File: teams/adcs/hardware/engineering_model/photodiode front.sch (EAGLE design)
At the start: 15 parts, among them U1 LTC2483IDD

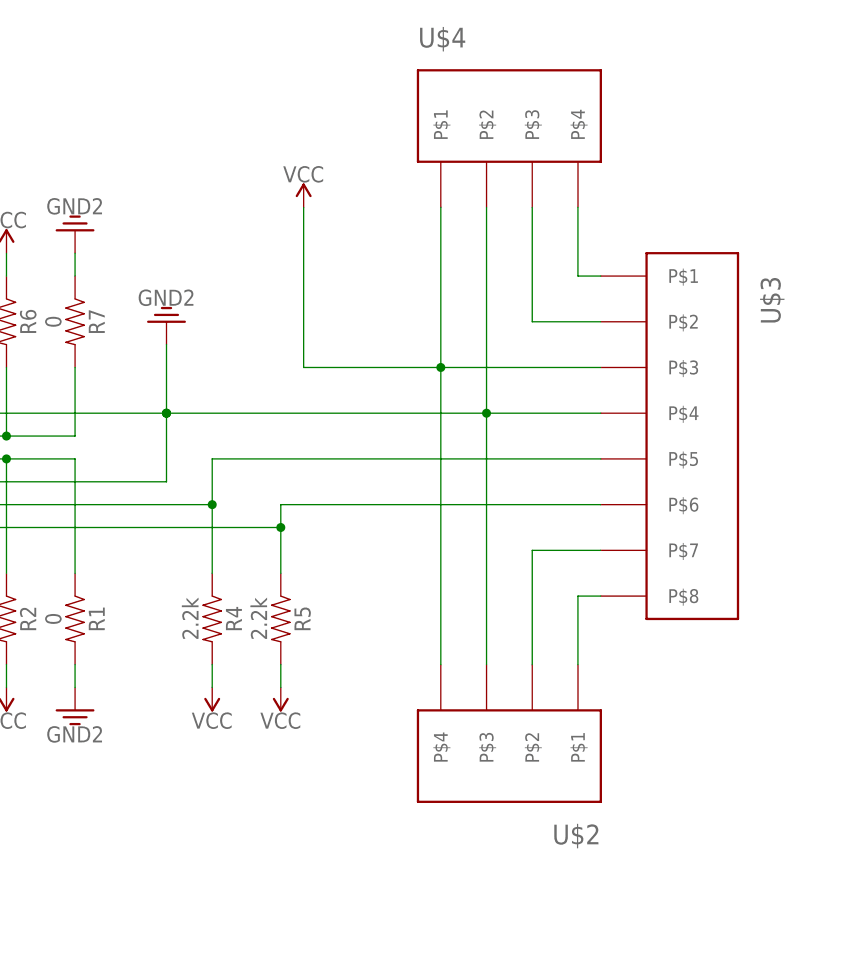
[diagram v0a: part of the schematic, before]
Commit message: Fixed front photodiode board
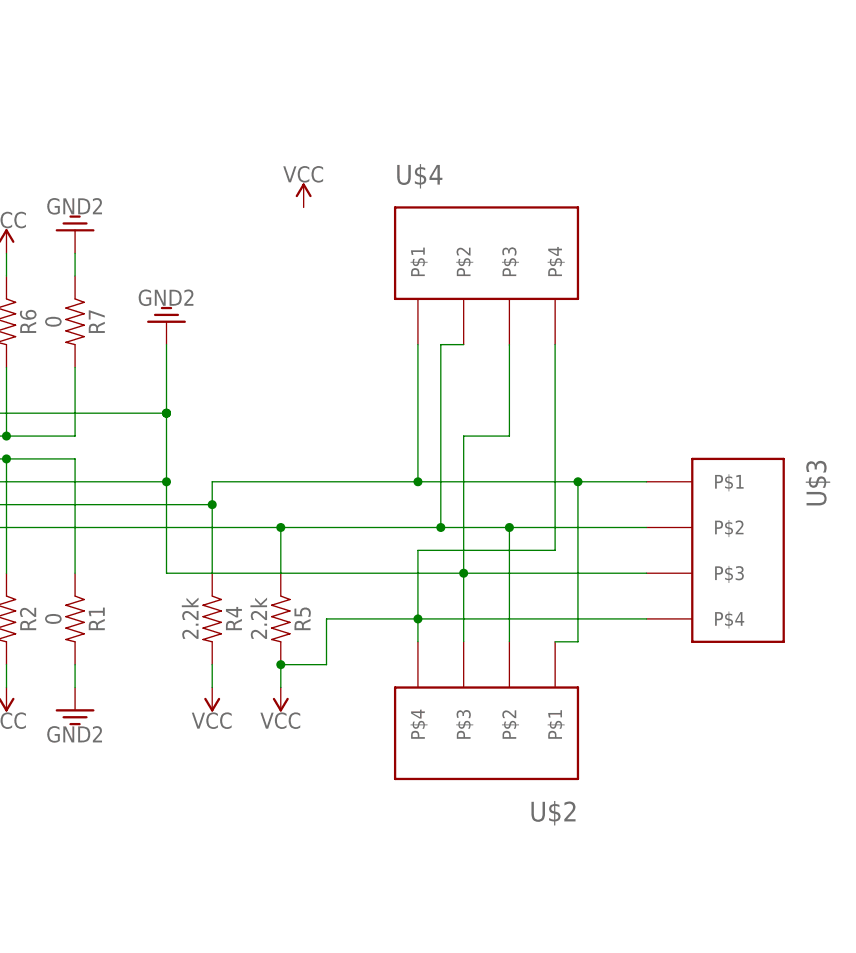
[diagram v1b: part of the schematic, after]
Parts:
- U$3: value PICOLOCK_8 -> PICOLOCK_4PICOLOCK_4; device DubSat1 Components:PICOLOCK_8 -> DubSat1 Components:PICOLOCK_4PICOLOCK_4
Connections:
- removed net N$1: U$3.P$2, U$4.P$3
- removed net N$2: U$3.P$1, U$4.P$4
- removed net N$3: U$2.P$1, U$3.P$8
- removed net N$4: U$2.P$2, U$3.P$7
- net GND: now also U$3.P$3, U$4.P$3; no longer U$3.P$4, U$4.P$2
- net SCL: now also U$2.P$2, U$3.P$2, U$4.P$2; no longer U$3.P$6
- net SDA: now also U$2.P$1, U$3.P$1, U$4.P$1; no longer U$3.P$5
- net VCC: now also U$3.P$4, U$4.P$4; no longer U$3.P$3, U$4.P$1
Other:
- moved on the sheet: U$2, U$4
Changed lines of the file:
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@@
 <part name="GND" library="SparkFun-PowerSymbols" deviceset="GND2" device=""/>
 <part name="C2" library="SparkFun-Capacitors" deviceset="0.1UF" device="-0603-100V-10%" value="1uF"/>
-<part name="U$3" library="DubSat1 Components" deviceset="PICOLOCK_8" device=""/>
 <part name="U$2" library="DubSat1 Components" deviceset="PICOLOCK_4" device="PICOLOCK_4"/>
 <part name="U$4" library="DubSat1 Components" deviceset="PICOLOCK_4" device="PICOLOCK_4"/>
 <part name="SUPPLY9" library="SparkFun-PowerSymbols" deviceset="VCC" device=""/>
+<part name="U$3" library="DubSat1 Components" deviceset="PICOLOCK_4" device="PICOLOCK_4"/>
 </parts>
 <sheets>
@@
 <instance part="GND" gate="G$1" x="129.54" y="78.74" rot="R180"/>
 <instance part="C2" gate="G$1" x="33.02" y="76.2"/>
-<instance part="U$3" gate="G$1" x="182.88" y="71.12" rot="R270"/>
-<instance part="U$2" gate="G$1" x="162.56" y="35.56" rot="R180"/>
-<instance part="U$4" gate="G$1" x="172.72" y="96.52"/>
+<instance part="U$2" gate="G$1" x="160.02" y="38.1" rot="R180"/>
+<instance part="U$4" gate="G$1" x="170.18" y="81.28"/>
 <instance part="SUPPLY9" gate="G$1" x="144.78" y="91.44"/>
+<instance part="U$3" gate="G$1" x="187.96" y="48.26" rot="R270"/>
 </instances>
 <busses>
@@
 <pinref part="SUPPLY5" gate="G$1" pin="VCC"/>
 <wire x1="142.24" y1="40.64" x2="142.24" y2="38.1" width="0.1524" layer="91"/>
-</segment>
-<segment>
-<pinref part="SUPPLY9" gate="G$1" pin="VCC"/>
-<pinref part="U$3" gate="G$1" pin="P$3"/>
-<wire x1="144.78" y1="91.44" x2="144.78" y2="73.66" width="0.1524" layer="91"/>
-<wire x1="144.78" y1="73.66" x2="160.02" y2="73.66" width="0.1524" layer="91"/>
-<pinref part="U$4" gate="G$1" pin="P$1"/>
-<wire x1="160.02" y1="73.66" x2="177.8" y2="73.66" width="0.1524" layer="91"/>
-<wire x1="160.02" y1="91.44" x2="160.02" y2="73.66" width="0.1524" layer="91"/>
-<junction x="160.02" y="73.66"/>
+<pinref part="U$3" gate="G$1" pin="P$4"/>
+<wire x1="157.48" y1="45.72" x2="147.32" y2="45.72" width="0.1524" layer="91"/>
+<wire x1="147.32" y1="45.72" x2="147.32" y2="40.64" width="0.1524" layer="91"/>
+<wire x1="147.32" y1="40.64" x2="142.24" y2="40.64" width="0.1524" layer="91"/>
+<junction x="142.24" y="40.64"/>
+<pinref part="U$4" gate="G$1" pin="P$4"/>
+<wire x1="172.72" y1="76.2" x2="172.72" y2="53.34" width="0.1524" layer="91"/>
 <pinref part="U$2" gate="G$1" pin="P$4"/>
-<wire x1="160.02" y1="40.64" x2="160.02" y2="73.66" width="0.1524" layer="91"/>
+<wire x1="172.72" y1="53.34" x2="157.48" y2="53.34" width="0.1524" layer="91"/>
+<wire x1="157.48" y1="53.34" x2="157.48" y2="45.72" width="0.1524" layer="91"/>
+<wire x1="157.48" y1="45.72" x2="157.48" y2="43.18" width="0.1524" layer="91"/>
+<wire x1="182.88" y1="45.72" x2="157.48" y2="45.72" width="0.1524" layer="91"/>
+<junction x="157.48" y="45.72"/>
 </segment>
 </net>
@@
 <pinref part="R5" gate="G$1" pin="1"/>
 <wire x1="142.24" y1="50.8" x2="142.24" y2="55.88" width="0.1524" layer="91"/>
-<pinref part="U$3" gate="G$1" pin="P$6"/>
-<wire x1="177.8" y1="58.42" x2="142.24" y2="58.42" width="0.1524" layer="91"/>
-<wire x1="142.24" y1="58.42" x2="142.24" y2="55.88" width="0.1524" layer="91"/>
+<pinref part="U$3" gate="G$1" pin="P$2"/>
+<wire x1="182.88" y1="55.88" x2="167.64" y2="55.88" width="0.1524" layer="91"/>
 <junction x="142.24" y="55.88"/>
+<pinref part="U$2" gate="G$1" pin="P$2"/>
+<wire x1="167.64" y1="55.88" x2="160.02" y2="55.88" width="0.1524" layer="91"/>
+<wire x1="160.02" y1="55.88" x2="142.24" y2="55.88" width="0.1524" layer="91"/>
+<wire x1="167.64" y1="43.18" x2="167.64" y2="55.88" width="0.1524" layer="91"/>
+<junction x="167.64" y="55.88"/>
+<pinref part="U$4" gate="G$1" pin="P$2"/>
+<wire x1="162.56" y1="76.2" x2="160.02" y2="76.2" width="0.1524" layer="91"/>
+<wire x1="160.02" y1="76.2" x2="160.02" y2="55.88" width="0.1524" layer="91"/>
+<junction x="160.02" y="55.88"/>
 </segment>
 </net>
@@
 <pinref part="R4" gate="G$1" pin="1"/>
 <wire x1="134.62" y1="50.8" x2="134.62" y2="58.42" width="0.1524" layer="91"/>
-<pinref part="U$3" gate="G$1" pin="P$5"/>
-<wire x1="177.8" y1="63.5" x2="134.62" y2="63.5" width="0.1524" layer="91"/>
-<wire x1="134.62" y1="63.5" x2="134.62" y2="58.42" width="0.1524" layer="91"/>
+<pinref part="U$3" gate="G$1" pin="P$1"/>
+<wire x1="182.88" y1="60.96" x2="175.26" y2="60.96" width="0.1524" layer="91"/>
+<wire x1="175.26" y1="60.96" x2="157.48" y2="60.96" width="0.1524" layer="91"/>
+<wire x1="157.48" y1="60.96" x2="134.62" y2="60.96" width="0.1524" layer="91"/>
+<wire x1="134.62" y1="60.96" x2="134.62" y2="58.42" width="0.1524" layer="91"/>
 <junction x="134.62" y="58.42"/>
+<pinref part="U$4" gate="G$1" pin="P$1"/>
+<wire x1="157.48" y1="76.2" x2="157.48" y2="60.96" width="0.1524" layer="91"/>
+<junction x="157.48" y="60.96"/>
+<pinref part="U$2" gate="G$1" pin="P$1"/>
+<wire x1="172.72" y1="43.18" x2="175.26" y2="43.18" width="0.1524" layer="91"/>
+<wire x1="175.26" y1="43.18" x2="175.26" y2="60.96" width="0.1524" layer="91"/>
+<junction x="175.26" y="60.96"/>
 </segment>
 </net>
@@
 <wire x1="109.22" y1="68.58" x2="129.54" y2="68.58" width="0.1524" layer="91"/>
 <junction x="129.54" y="68.58"/>
-<pinref part="U$3" gate="G$1" pin="P$4"/>
-<wire x1="177.8" y1="68.58" x2="165.1" y2="68.58" width="0.1524" layer="91"/>
+<pinref part="U$3" gate="G$1" pin="P$3"/>
+<wire x1="162.56" y1="50.8" x2="129.54" y2="50.8" width="0.1524" layer="91"/>
+<wire x1="129.54" y1="50.8" x2="129.54" y2="60.96" width="0.1524" layer="91"/>
+<junction x="129.54" y="60.96"/>
 <pinref part="U$2" gate="G$1" pin="P$3"/>
-<wire x1="165.1" y1="68.58" x2="129.54" y2="68.58" width="0.1524" layer="91"/>
-<wire x1="165.1" y1="40.64" x2="165.1" y2="68.58" width="0.1524" layer="91"/>
-<junction x="165.1" y="68.58"/>
-<pinref part="U$4" gate="G$1" pin="P$2"/>
-<wire x1="165.1" y1="91.44" x2="165.1" y2="68.58" width="0.1524" layer="91"/>
+<wire x1="162.56" y1="43.18" x2="162.56" y2="50.8" width="0.1524" layer="91"/>
+<pinref part="U$4" gate="G$1" pin="P$3"/>
+<wire x1="162.56" y1="50.8" x2="162.56" y2="66.04" width="0.1524" layer="91"/>
+<wire x1="162.56" y1="66.04" x2="167.64" y2="66.04" width="0.1524" layer="91"/>
+<wire x1="167.64" y1="66.04" x2="167.64" y2="76.2" width="0.1524" layer="91"/>
+<wire x1="182.88" y1="50.8" x2="162.56" y2="50.8" width="0.1524" layer="91"/>
+<junction x="162.56" y="50.8"/>
 </segment>
 <segment>
@@
 </segment>
 </net>
-<net name="N$1" class="0">
-<segment>
-<pinref part="U$3" gate="G$1" pin="P$2"/>
-<pinref part="U$4" gate="G$1" pin="P$3"/>
-<wire x1="177.8" y1="78.74" x2="170.18" y2="78.74" width="0.1524" layer="91"/>
-<wire x1="170.18" y1="78.74" x2="170.18" y2="91.44" width="0.1524" layer="91"/>
-</segment>
-</net>
-<net name="N$2" class="0">
-<segment>
-<pinref part="U$3" gate="G$1" pin="P$1"/>
-<pinref part="U$4" gate="G$1" pin="P$4"/>
-<wire x1="177.8" y1="83.82" x2="175.26" y2="83.82" width="0.1524" layer="91"/>
-<wire x1="175.26" y1="83.82" x2="175.26" y2="91.44" width="0.1524" layer="91"/>
-</segment>
-</net>
-<net name="N$3" class="0">
-<segment>
-<pinref part="U$3" gate="G$1" pin="P$8"/>
-<pinref part="U$2" gate="G$1" pin="P$1"/>
-<wire x1="177.8" y1="48.26" x2="175.26" y2="48.26" width="0.1524" layer="91"/>
-<wire x1="175.26" y1="48.26" x2="175.26" y2="40.64" width="0.1524" layer="91"/>
-</segment>
-</net>
-<net name="N$4" class="0">
-<segment>
-<pinref part="U$3" gate="G$1" pin="P$7"/>
-<pinref part="U$2" gate="G$1" pin="P$2"/>
-<wire x1="177.8" y1="53.34" x2="170.18" y2="53.34" width="0.1524" layer="91"/>
-<wire x1="170.18" y1="53.34" x2="170.18" y2="40.64" width="0.1524" layer="91"/>
-</segment>
-</net>

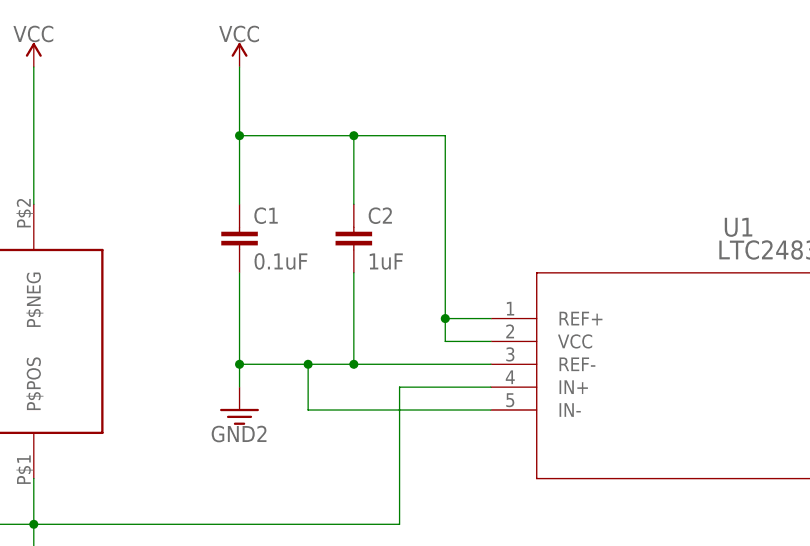
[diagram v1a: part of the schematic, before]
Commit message: Photodiode front board changes: same hole locations as before, 2x extra picolock connectors to go to side boards, capacitors changed from 0603 to 0805, smoothing capacitors moved next to power input of ADC, and i2c pullups moved onto the top of the board to be easily removed
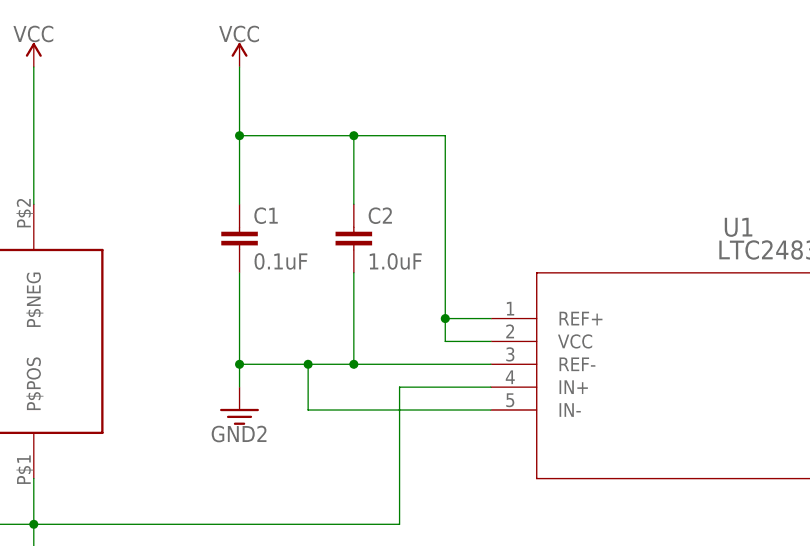
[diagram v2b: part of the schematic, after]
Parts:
- C1, C6: device SparkFun-Capacitors:0.1UF-0603-100V-10% -> SparkFun-Capacitors:10UF-0805-10V-10%
- C2: value 1uF -> 1.0uF; device SparkFun-Capacitors:0.1UF-0603-100V-10% -> SparkFun-Capacitors:10UF-0805-10V-10%
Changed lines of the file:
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@@
 <part name="SUPPLY3" library="SparkFun-PowerSymbols" deviceset="VCC" device=""/>
 <part name="GND6" library="SparkFun-PowerSymbols" deviceset="GND2" device=""/>
-<part name="C6" library="SparkFun-Capacitors" deviceset="0.1UF" device="-0603-100V-10%" value="0.1uF"/>
+<part name="C6" library="SparkFun-Capacitors" library_urn="urn:adsk.eagle:library:510" deviceset="10UF" device="-0805-10V-10%" package3d_urn="urn:adsk.eagle:package:37429/1" value="0.1uF"/>
 <part name="R3" library="SparkFun-Resistors" deviceset="RESISTOR" device="0805" value="800"/>
 <part name="GND8" library="SparkFun-PowerSymbols" deviceset="GND2" device=""/>
 <part name="GND9" library="SparkFun-PowerSymbols" deviceset="GND2" device=""/>
 <part name="U$1" library="SFH 2430 Z" deviceset="SFH-2430-Z" device=""/>
-<part name="C1" library="SparkFun-Capacitors" deviceset="0.1UF" device="-0603-100V-10%" value="0.1uF"/>
+<part name="C1" library="SparkFun-Capacitors" library_urn="urn:adsk.eagle:library:510" deviceset="10UF" device="-0805-10V-10%" package3d_urn="urn:adsk.eagle:package:37429/1" value="0.1uF"/>
 <part name="R1" library="SparkFun-Resistors" deviceset="RESISTOR" device="0805" value="0"/>
 <part name="R2" library="SparkFun-Resistors" deviceset="RESISTOR" device="0805" value="0"/>
@@
 <part name="R5" library="SparkFun-Resistors" deviceset="RESISTOR" device="0805" value="2.2k"/>
 <part name="GND" library="SparkFun-PowerSymbols" deviceset="GND2" device=""/>
-<part name="C2" library="SparkFun-Capacitors" deviceset="0.1UF" device="-0603-100V-10%" value="1uF"/>
+<part name="C2" library="SparkFun-Capacitors" library_urn="urn:adsk.eagle:library:510" deviceset="10UF" device="-0805-10V-10%" package3d_urn="urn:adsk.eagle:package:37429/1" value="1.0uF"/>
 <part name="U$2" library="DubSat1 Components" deviceset="PICOLOCK_4" device="PICOLOCK_4"/>
 <part name="U$4" library="DubSat1 Components" deviceset="PICOLOCK_4" device="PICOLOCK_4"/>
@@
 </schematic>
 </drawing>
+<compatibility>
+<note version="8.2" severity="warning">
+Since Version 8.2, EAGLE supports online libraries. The ids
+of those online libraries will not be understood (or retained)
+with this version.
+</note>
+<note version="8.3" severity="warning">
+Since Version 8.3, EAGLE supports URNs for individual library
+assets (packages, symbols, and devices). The URNs of those assets
+will not be understood (or retained) with this version.
+</note>
+<note version="8.3" severity="warning">
+Since Version 8.3, EAGLE supports the association of 3D packages
+with devices in libraries, schematics, and board files. Those 3D
+packages will not be understood (or retained) with this version.
+</note>
+</compatibility>
 </eagle>
